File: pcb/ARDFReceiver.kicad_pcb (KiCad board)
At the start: 2 copper layers, 60 x 75 mm, 97 parts, among them J1 Conn_01x02_MountingPin, J2 Conn_01x04_MountingPin, J3 Conn_Coaxial, J4 AudioJack3, P1 SSD1306 Pin, Q1 BSS138, Q2 BSS84, Q3 BSS138, Q4 2SC5066-Y, U1 XIAO-ESP32-C6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

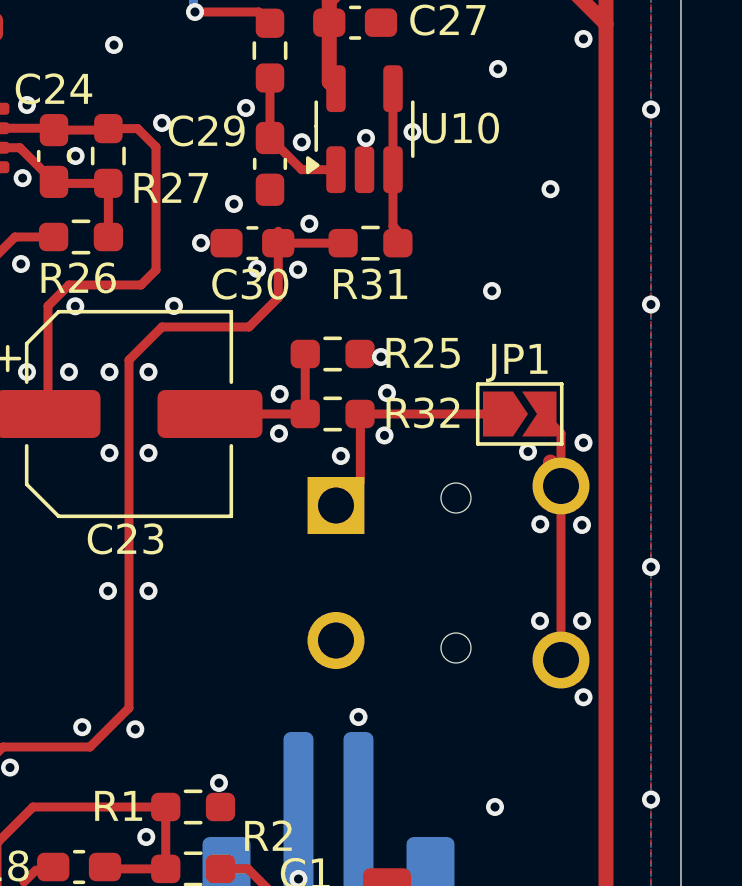
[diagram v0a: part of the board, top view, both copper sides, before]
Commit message: Adjust positions of 3.5mm Jack and Solder Jumper
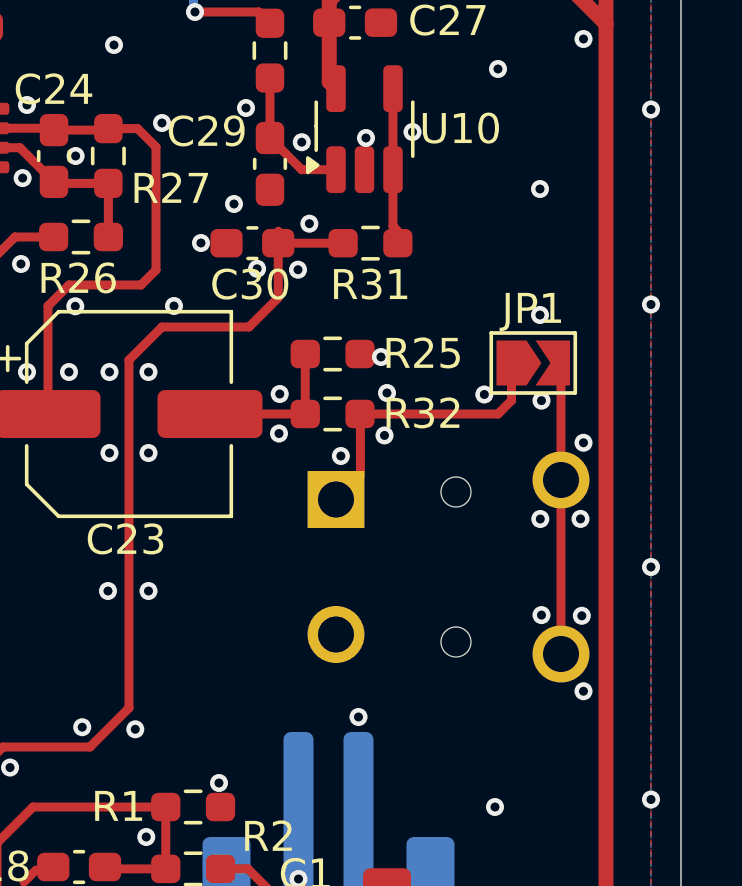
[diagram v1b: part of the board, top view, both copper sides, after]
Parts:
- moved JP1 1.76 mm to (105.1, 98.2)
- moved J4 0.20 mm to (105.0, 105.0)
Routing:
- net Net-(JP1-A): track 7.99 -> 9.68 mm
- net Net-(JP1-B): track 9.32 -> 10.6 mm
- net GND: vias 339 -> 340
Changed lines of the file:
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@@
 	(footprint "Jumper:SolderJumper-2_P1.3mm_Open_TrianglePad1.0x1.5mm"
 		(layer "F.Cu")
-		(at 104.625 99.9)
+		(at 105.075 98.2)
 		(descr "SMD Solder Jumper, 1x1.5mm Triangular Pads, 0.3mm gap, open")
 		(tags "solder jumper open")
@@
 	(footprint "Connector_Audio:Jack_3.5mm_Switronic_ST-005-G_horizontal"
 		(layer "B.Cu")
-		(at 105 105.2 180)
+		(at 105 105 180)
 		(descr "3.5mm horizontal headphones jack, http://akizukidenshi.com/download/ds/switronic/ST-005-G.pdf")
 		(tags "Connector Audio Switronic ST-005-G")
@@
 	)
 	(via
-		(at 105.3 106.8)
+		(at 105.35 106.603078)
 		(size 0.6)
 		(drill 0.3)
@@
 	)
 	(via
-		(at 104.900238 101.155)
+		(at 105.35 99.455)
 		(size 0.6)
 		(drill 0.3)
@@
 	)
 	(via
+		(at 103.443837 99.25)
+		(size 0.6)
+		(drill 0.3)
+		(layers "F.Cu" "B.Cu")
+		(free yes)
+		(net 3)
+	)
+	(via
 		(at 94.4 85.6)
 		(size 0.6)
@@
 	)
 	(via
-		(at 106.75 109.340969)
+		(at 106.75 109.140969)
 		(size 0.6)
 		(drill 0.3)
@@
 	)
 	(via
-		(at 106.7 106.8)
+		(at 106.694337 106.627049)
 		(size 0.6)
 		(drill 0.3)
@@
 	)
 	(via
-		(at 106.7 103.6)
+		(at 106.65 103.396922)
 		(size 0.6)
 		(drill 0.3)
@@
 	)
 	(via
-		(at 105.65 92.40625)
+		(at 105.3 92.4)
 		(size 0.6)
 		(drill 0.3)
@@
 	)
 	(via
-		(at 103.7 95.8)
+		(at 105.3 96.6)
 		(size 0.6)
 		(drill 0.3)
@@
 	)
 	(via
-		(at 105.309388 103.574975)
+		(at 105.309388 103.4)
 		(size 0.6)
 		(drill 0.3)
@@
 	)
 	(segment
+		(start 99.3135 99.9135)
+		(end 99.3135 101.9365)
+		(width 0.3)
+		(layer "F.Cu")
+		(net 63)
+	)
+	(segment
+		(start 99.3 99.9)
+		(end 99.3135 99.9135)
+		(width 0.3)
+		(layer "F.Cu")
+		(net 63)
+	)
+	(segment
+		(start 104.35 99.45)
+		(end 104.35 98.2)
+		(width 0.3)
+		(layer "F.Cu")
+		(net 63)
+	)
+	(segment
 		(start 99.3 99.9)
 		(end 103.9 99.9)
@@
 	)
 	(segment
-		(start 99.3125 102.1375)
-		(end 98.5 102.95)
+		(start 99.3135 101.9365)
+		(end 98.5 102.75)
 		(width 0.3)
 		(layer "F.Cu")
@@
 	)
 	(segment
-		(start 99.3125 99.9)
-		(end 99.3125 102.1375)
+		(start 103.9 99.9)
+		(end 104.35 99.45)
 		(width 0.3)
 		(layer "F.Cu")
@@
 	)
 	(segment
-		(start 105.35 99.9)
-		(end 106 100.55)
+		(start 106 98.4)
+		(end 105.8 98.2)
 		(width 0.3)
 		(layer "F.Cu")
@@
 	)
 	(segment
-		(start 106 102.3)
-		(end 106 108.1)
+		(start 106 102.1)
+		(end 106 98.4)
 		(width 0.3)
 		(layer "F.Cu")
@@
 	)
 	(segment
-		(start 106 100.55)
-		(end 106 102.3)
+		(start 106 102.1)
+		(end 106 107.9)
 		(width 0.3)
 		(layer "F.Cu")
